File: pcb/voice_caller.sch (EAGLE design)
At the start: 36 parts, among them IC1 PRO_MICRO, IC3 78L12SMD, K1 TQ2SA-L2-5V, U1 25F32006WSOI

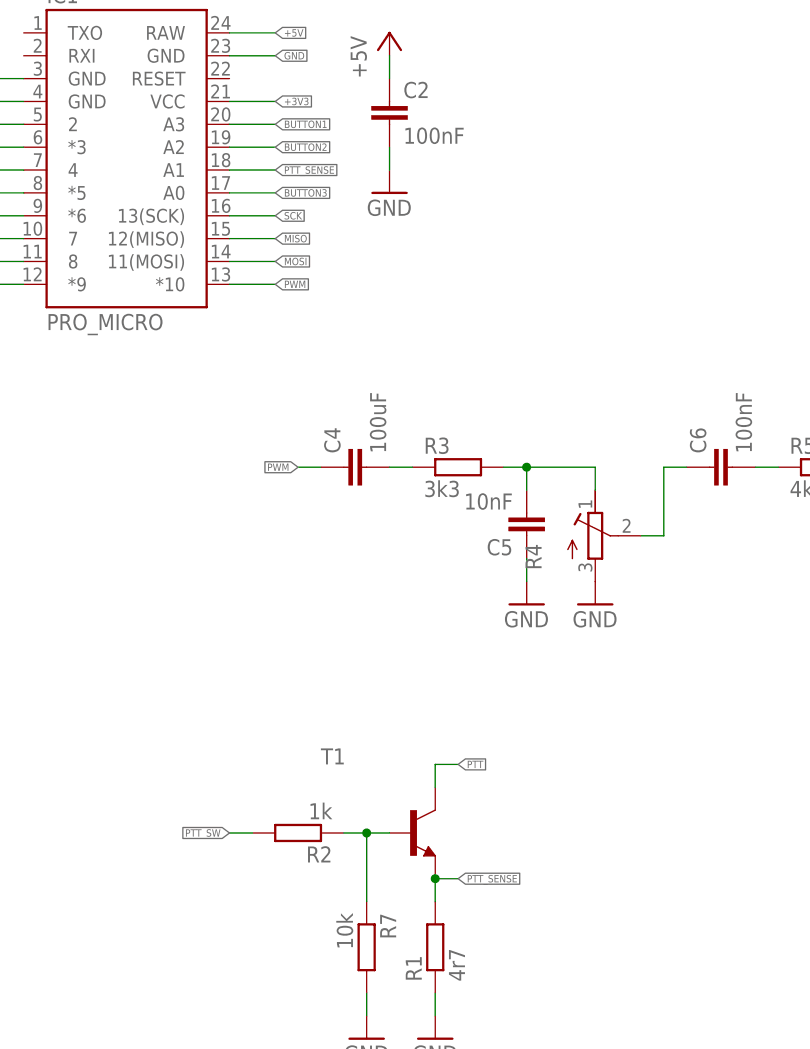
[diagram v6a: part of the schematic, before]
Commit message: Flash routed, PTT sense changed.
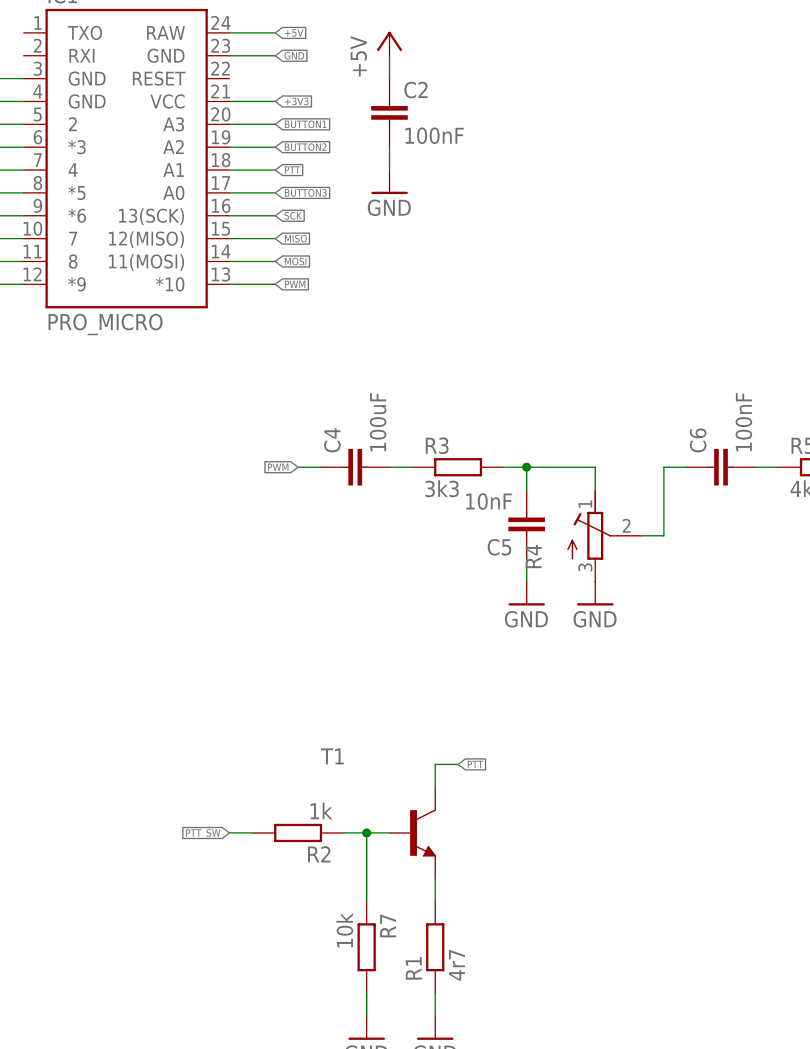
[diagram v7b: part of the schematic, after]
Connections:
- net PTT: now also IC1.A1
- net PTT_SENSE: no longer IC1.A1
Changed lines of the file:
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@@
 <label x="86.36" y="76.2" size="0.8128" layer="95" xref="yes"/>
+</segment>
+<segment>
+<pinref part="IC1" gate="G$1" pin="A1"/>
+<wire x1="60.96" y1="142.24" x2="66.04" y2="142.24" width="0.1524" layer="91"/>
+<label x="66.04" y="142.24" size="0.8128" layer="95" xref="yes"/>
 </segment>
 </net>
@@
 <pinref part="R1" gate="G$1" pin="2"/>
 <wire x1="83.82" y1="60.96" x2="83.82" y2="63.5" width="0.1524" layer="91"/>
-<wire x1="83.82" y1="63.5" x2="86.36" y2="63.5" width="0.1524" layer="91"/>
-<junction x="83.82" y="63.5"/>
-<label x="86.36" y="63.5" size="0.8128" layer="95" xref="yes"/>
-</segment>
-<segment>
-<pinref part="IC1" gate="G$1" pin="A1"/>
-<wire x1="60.96" y1="142.24" x2="66.04" y2="142.24" width="0.1524" layer="91"/>
-<label x="66.04" y="142.24" size="0.8128" layer="95" xref="yes"/>
-</segment>
-</net>
+</segment>
+</net>

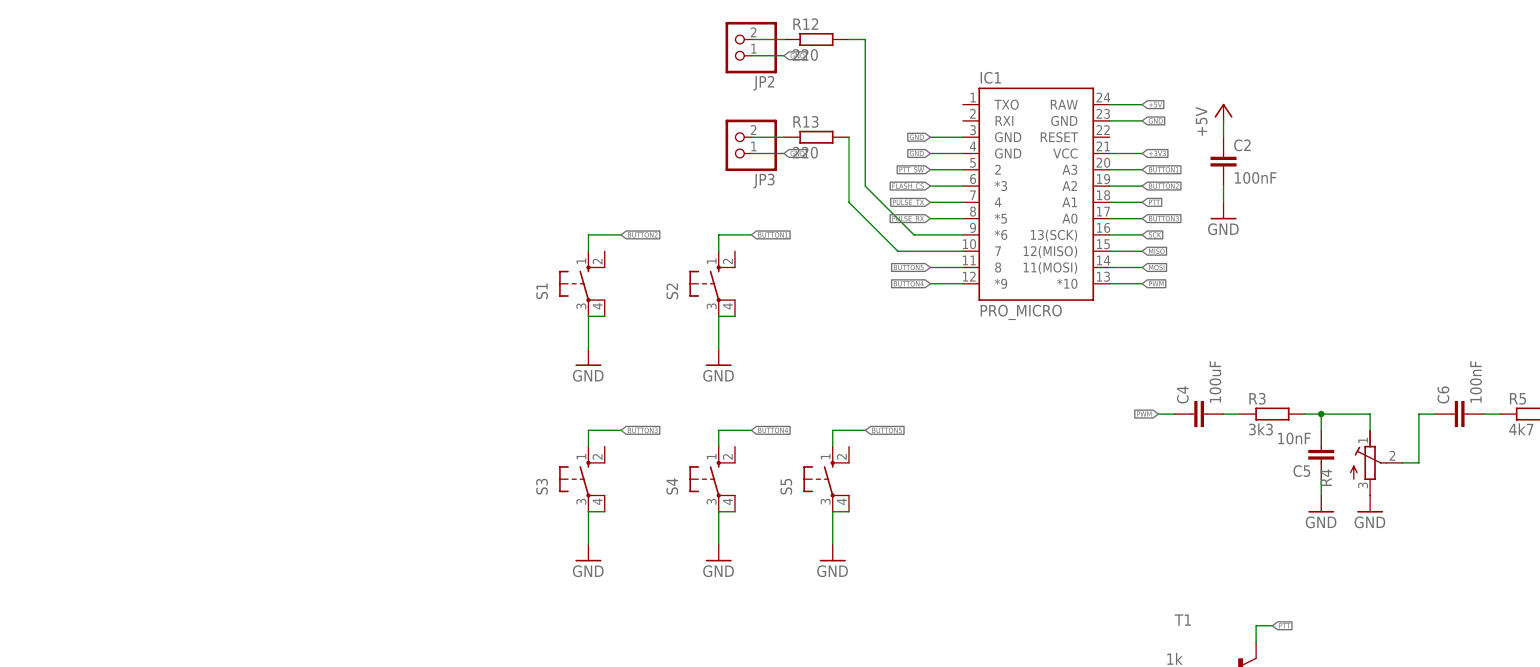
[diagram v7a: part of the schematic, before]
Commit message: Monitor amp added and routed.
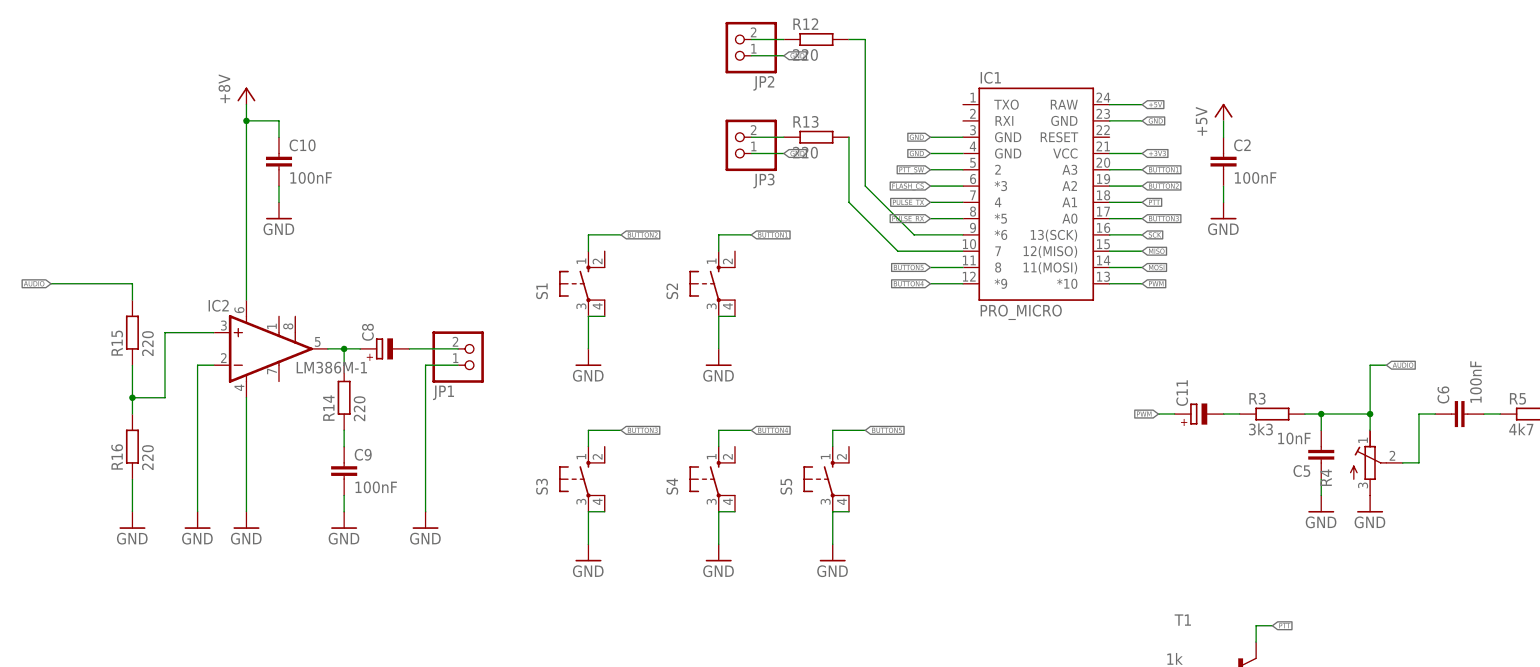
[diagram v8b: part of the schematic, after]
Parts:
- removed C4: 100uF, rcl:C-EUC1206K
- added C10, C9: 100nF, rcl:C-EUC1206K
- added C11, C8: (no value), rcl:CPOL-EUE2.5-6
- added IC2: LM386M-1, linear:LM386M-1
- added JP1: (no value), pinhead:PINHD-1X2
- added R14, R15, R16: 220, rcl:R-EU_M1206
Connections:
- new net AUDIO: C5.2, R15.2, R3.2, R4.E
- new net N$16: C8.+, IC2.OUT, R14.2
- new net N$21: C9.1, R14.1
- new net N$22: C8.-, JP1.2
- new net VCC: C10.1, IC2.VS
- net GND: now also C10.2, C9.2, IC2.-IN, IC2.GND, JP1.1, R16.1
- net N$1: now also C11.-; no longer C4.2
- net N$2: now also IC2.+IN, R15.1, R16.2; no longer C5.2, R3.2, R4.E
- net PWM: now also C11.+; no longer C4.1
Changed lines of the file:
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@@
 <part name="GND5" library="supply1" deviceset="GND" device=""/>
 <part name="GND6" library="supply1" deviceset="GND" device=""/>
-<part name="C4" library="rcl" deviceset="C-EU" device="C1206K" value="100uF"/>
 <part name="R3" library="rcl" deviceset="R-EU_" device="M1206" value="3k3"/>
 <part name="C5" library="rcl" deviceset="C-EU" device="C1206K" value="10nF"/>
@@
 <part name="JP3" library="pinhead" deviceset="PINHD-1X2" device=""/>
 <part name="U1" library="SparkFun-IC-Memory" deviceset="SPI_FLASH-X25XX" device="SMD1" value="25F32006WSOI"/>
+<part name="IC2" library="linear" deviceset="LM386?-*" device="M" technology="1"/>
+<part name="C8" library="rcl" deviceset="CPOL-EU" device="E2.5-6"/>
+<part name="GND20" library="supply1" deviceset="GND" device=""/>
+<part name="R14" library="rcl" deviceset="R-EU_" device="M1206" value="220"/>
+<part name="C9" library="rcl" deviceset="C-EU" device="C1206K" value="100nF"/>
+<part name="GND21" library="supply1" deviceset="GND" device=""/>
+<part name="JP1" library="pinhead" deviceset="PINHD-1X2" device=""/>
+<part name="GND22" library="supply1" deviceset="GND" device=""/>
+<part name="+8V1" library="supply1" deviceset="VCC" device="" value="+8V"/>
+<part name="C10" library="rcl" deviceset="C-EU" device="C1206K" value="100nF"/>
+<part name="GND23" library="supply1" deviceset="GND" device=""/>
+<part name="GND24" library="supply1" deviceset="GND" device=""/>
+<part name="GND25" library="supply1" deviceset="GND" device=""/>
+<part name="R15" library="rcl" deviceset="R-EU_" device="M1206" value="220"/>
+<part name="R16" library="rcl" deviceset="R-EU_" device="M1206" value="220"/>
+<part name="C11" library="rcl" deviceset="CPOL-EU" device="E2.5-6"/>
 </parts>
 <sheets>
@@
 <instance part="GND5" gate="1" x="-20.32" y="116.84"/>
 <instance part="GND6" gate="1" x="154.94" y="99.06"/>
-<instance part="C4" gate="G$1" x="73.66" y="109.22" rot="R90"/>
 <instance part="R3" gate="G$1" x="86.36" y="109.22"/>
 <instance part="C5" gate="G$1" x="93.98" y="101.6" rot="R180"/>
@@
 <instance part="JP3" gate="G$1" x="2.54" y="152.4" rot="R180"/>
 <instance part="U1" gate="G$1" x="157.48" y="86.36"/>
+<instance part="IC2" gate="G$1" x="-71.12" y="119.38"/>
+<instance part="C8" gate="G$1" x="-53.34" y="119.38" rot="R90"/>
+<instance part="GND20" gate="1" x="-73.66" y="91.44"/>
+<instance part="R14" gate="G$1" x="-58.42" y="111.76" rot="R90"/>
+<instance part="C9" gate="G$1" x="-58.42" y="101.6"/>
+<instance part="GND21" gate="1" x="-58.42" y="91.44"/>
+<instance part="JP1" gate="G$1" x="-38.1" y="119.38" rot="MR180"/>
+<instance part="GND22" gate="1" x="-45.72" y="91.44"/>
+<instance part="+8V1" gate="VCC" x="-73.66" y="160.02"/>
+<instance part="C10" gate="G$1" x="-68.58" y="149.86"/>
+<instance part="GND23" gate="1" x="-68.58" y="139.7"/>
+<instance part="GND24" gate="1" x="-81.28" y="91.44"/>
+<instance part="GND25" gate="1" x="-91.44" y="91.44"/>
+<instance part="R15" gate="G$1" x="-91.44" y="121.92" rot="R90"/>
+<instance part="R16" gate="G$1" x="-91.44" y="104.14" rot="R90"/>
+<instance part="C11" gate="G$1" x="73.66" y="109.22" rot="R90"/>
 </instances>
 <busses>
@@
 <label x="139.7" y="81.28" size="0.8128" layer="95" rot="R180" xref="yes"/>
 </segment>
+<segment>
+<pinref part="IC2" gate="G$1" pin="GND"/>
+<wire x1="-73.66" y1="111.76" x2="-73.66" y2="93.98" width="0.1524" layer="91"/>
+<pinref part="GND20" gate="1" pin="GND"/>
+</segment>
+<segment>
+<pinref part="C9" gate="G$1" pin="2"/>
+<pinref part="GND21" gate="1" pin="GND"/>
+<wire x1="-58.42" y1="93.98" x2="-58.42" y2="96.52" width="0.1524" layer="91"/>
+</segment>
+<segment>
+<pinref part="JP1" gate="G$1" pin="1"/>
+<wire x1="-40.64" y1="116.84" x2="-45.72" y2="116.84" width="0.1524" layer="91"/>
+<wire x1="-45.72" y1="116.84" x2="-45.72" y2="93.98" width="0.1524" layer="91"/>
+<pinref part="GND22" gate="1" pin="GND"/>
+</segment>
+<segment>
+<pinref part="C10" gate="G$1" pin="2"/>
+<pinref part="GND23" gate="1" pin="GND"/>
+<wire x1="-68.58" y1="142.24" x2="-68.58" y2="144.78" width="0.1524" layer="91"/>
+</segment>
+<segment>
+<pinref part="IC2" gate="G$1" pin="-IN"/>
+<wire x1="-78.74" y1="116.84" x2="-81.28" y2="116.84" width="0.1524" layer="91"/>
+<pinref part="GND24" gate="1" pin="GND"/>
+<wire x1="-81.28" y1="93.98" x2="-81.28" y2="116.84" width="0.1524" layer="91"/>
+</segment>
+<segment>
+<pinref part="GND25" gate="1" pin="GND"/>
+<wire x1="-91.44" y1="93.98" x2="-91.44" y2="99.06" width="0.1524" layer="91"/>
+<pinref part="R16" gate="G$1" pin="1"/>
+</segment>
 </net>
 <net name="MOSI" class="0">
@@
 </segment>
 <segment>
-<pinref part="C4" gate="G$1" pin="1"/>
 <wire x1="71.12" y1="109.22" x2="68.58" y2="109.22" width="0.1524" layer="91"/>
 <label x="68.58" y="109.22" size="0.8128" layer="95" rot="R180" xref="yes"/>
+<pinref part="C11" gate="G$1" pin="+"/>
 </segment>
 </net>
 <net name="N$1" class="0">
 <segment>
-<pinref part="C4" gate="G$1" pin="2"/>
 <pinref part="R3" gate="G$1" pin="1"/>
 <wire x1="81.28" y1="109.22" x2="78.74" y2="109.22" width="0.1524" layer="91"/>
-</segment>
-</net>
-<net name="N$2" class="0">
+<pinref part="C11" gate="G$1" pin="-"/>
+</segment>
+</net>
+<net name="AUDIO" class="0">
 <segment>
 <pinref part="R3" gate="G$1" pin="2"/>
@@
 <pinref part="R4" gate="G$1" pin="E"/>
 <wire x1="101.6" y1="109.22" x2="101.6" y2="106.68" width="0.1524" layer="91"/>
+<label x="104.14" y="116.84" size="0.8128" layer="95" xref="yes"/>
+<wire x1="101.6" y1="109.22" x2="101.6" y2="116.84" width="0.1524" layer="91"/>
+<wire x1="101.6" y1="116.84" x2="104.14" y2="116.84" width="0.1524" layer="91"/>
+<junction x="101.6" y="109.22"/>
+</segment>
+<segment>
+<wire x1="-91.44" y1="127" x2="-91.44" y2="129.54" width="0.1524" layer="91"/>
+<wire x1="-91.44" y1="129.54" x2="-104.14" y2="129.54" width="0.1524" layer="91"/>
+<label x="-104.14" y="129.54" size="0.8128" layer="95" rot="R180" xref="yes"/>
+<pinref part="R15" gate="G$1" pin="2"/>
 </segment>
 </net>
@@
 </segment>
 </net>
+<net name="N$16" class="0">
+<segment>
+<pinref part="IC2" gate="G$1" pin="OUT"/>
+<wire x1="-60.96" y1="119.38" x2="-58.42" y2="119.38" width="0.1524" layer="91"/>
+<pinref part="C8" gate="G$1" pin="+"/>
+<pinref part="R14" gate="G$1" pin="2"/>
+<wire x1="-58.42" y1="119.38" x2="-55.88" y2="119.38" width="0.1524" layer="91"/>
+<wire x1="-58.42" y1="116.84" x2="-58.42" y2="119.38" width="0.1524" layer="91"/>
+<junction x="-58.42" y="119.38"/>
+</segment>
+</net>
+<net name="N$21" class="0">
+<segment>
+<pinref part="R14" gate="G$1" pin="1"/>
+<pinref part="C9" gate="G$1" pin="1"/>
+<wire x1="-58.42" y1="104.14" x2="-58.42" y2="106.68" width="0.1524" layer="91"/>
+</segment>
+</net>
+<net name="N$22" class="0">
+<segment>
+<pinref part="C8" gate="G$1" pin="-"/>
+<pinref part="JP1" gate="G$1" pin="2"/>
+<wire x1="-48.26" y1="119.38" x2="-40.64" y2="119.38" width="0.1524" layer="91"/>
+</segment>
+</net>
+<net name="VCC" class="0">
+<segment>
+<pinref part="IC2" gate="G$1" pin="VS"/>
+<wire x1="-73.66" y1="127" x2="-73.66" y2="154.94" width="0.1524" layer="91"/>
+<pinref part="+8V1" gate="VCC" pin="VCC"/>
+<pinref part="C10" gate="G$1" pin="1"/>
+<wire x1="-73.66" y1="154.94" x2="-73.66" y2="157.48" width="0.1524" layer="91"/>
+<wire x1="-68.58" y1="152.4" x2="-68.58" y2="154.94" width="0.1524" layer="91"/>
+<wire x1="-68.58" y1="154.94" x2="-73.66" y2="154.94" width="0.1524" layer="91"/>
+<junction x="-73.66" y="154.94"/>
+</segment>
+</net>
+<net name="N$2" class="0">
+<segment>
+<pinref part="IC2" gate="G$1" pin="+IN"/>
+<wire x1="-78.74" y1="121.92" x2="-86.36" y2="121.92" width="0.1524" layer="91"/>
+<wire x1="-86.36" y1="121.92" x2="-86.36" y2="111.76" width="0.1524" layer="91"/>
+<pinref part="R15" gate="G$1" pin="1"/>
+<pinref part="R16" gate="G$1" pin="2"/>
+<wire x1="-91.44" y1="116.84" x2="-91.44" y2="111.76" width="0.1524" layer="91"/>
+<wire x1="-91.44" y1="111.76" x2="-91.44" y2="109.22" width="0.1524" layer="91"/>
+<wire x1="-86.36" y1="111.76" x2="-91.44" y2="111.76" width="0.1524" layer="91"/>
+<junction x="-91.44" y="111.76"/>
+</segment>
+</net>
